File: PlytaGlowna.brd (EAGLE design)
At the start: 80 x 50 mm, 17 parts, among them X10A- CZUJ_STOP_PRAWY, X11A- CZUJNIK_STOP_LEWY, X12A- SWIATL_PRZOD, X13A- SWIATL_TYL, X1B 5566-2, X2A- STACYJKA, X3A- VOLTOMIERZ, X4A- PRZERYWACZ, X5A- WL_SWIATLA_DZIENNE, X6A- REKOJESC_LEW, X7A- KLAKSON, X8A- ZAS USB/12V, X9A- SYGNALIZATOR

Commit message: druga wyprodukowana plytka
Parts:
- removed R1, R2, R3, R4: (no value), rcl:R1206
- removed X5A-: WL_SWIATLA_DZIENNE, my_electronics_library:PCB-43045-0212
- added D1, D2: 1N4446, diode:DO35-10
- added U$1: 43045-0412, my_electronics_library:PCB-43045-0412
- added U$2: BUZZER, my_electronics_library:PCB-43045-0212
- moved X11A- 13.0 mm to (43.0, 9.00)
- moved X10A- 10.0 mm to (34.0, 9.00)
- moved X4A- 4.00 mm to (10.0, 38.0)
- moved X9A- 3.00 mm to (41.0, 25.0)
- moved X7A- 1.00 mm to (28.4, 23.8)
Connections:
- removed net N$2: R2.2, X9A-.P$2
- removed net N$3: R3.2, X9A-.P$3
- removed net N$4: R4.2, X9A-.P$5
- net +12V: no longer X6A-.P$4
- net +12V/ST: now also U$1.P$2, X6A-.P$4, X9A-.P$5; no longer R4.1, X5A-.P$1
- net DZIENNE: now also U$1.P$1; no longer X5A-.P$2
- net KIER_LEWY: now also D1.A, X9A-.P$1; no longer R1.1
- net KIER_PRAWY: now also D2.A, X9A-.P$2; no longer R2.1
- net MASA: now also U$1.P$3, U$2.P$2
- net MIJANIA: now also X9A-.P$3; no longer R3.1
- net N$1: now also D1.C, D2.C, U$2.P$1; no longer R1.2, X9A-.P$1
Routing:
- net +12V: track 57.9 -> 28.6 mm, vias 2 -> 0
- net N$1: track 13.9 -> 38.8 mm
- net MASA: track 205.9 -> 224.0 mm
- net STOP: track 24.2 -> 39.1 mm
- net KIER_LEWY: track 93.9 -> 105.9 mm, vias 2 -> 3
- net KIER_PRAWY: track 102.4 -> 114.0 mm
- net MIJANIA: track 70.4 -> 79.2 mm
- net N$4: track 6.21 -> 0.00 mm
- net N$3: track 5.08 -> 0.00 mm
- net N$2: track 5.04 -> 0.00 mm
- net DZIENNE: track 13.8 -> 18.8 mm
- net KIER_WSPOLNY: track 28.1 -> 32.1 mm
- net +12V/ST: track 148.3 -> 145.8 mm
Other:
- board text added: "rev. 002"

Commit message: czesc zmian do wersji 3
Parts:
- removed U$2: BUZZER, my_electronics_library:PCB-43045-0212
- removed X2A-: STACYJKA, my_electronics_library:PCB-43045-0212
- removed X3A-: VOLTOMIERZ, my_electronics_library:PCB-43045-0212
- removed X4A-: PRZERYWACZ, my_electronics_library:PCB-43045-0412
- added J1: PRZERYWACZ, con-molex:6410-03
- added J2: STACYJKA, con-molex:6410-02
- added J3: VOLTOMIERZ, con-molex:6410-02
- added J4: BUZZER, con-molex:6410-02
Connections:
- net +12V: now also J2.1; no longer X2A-.P$1
- net +12V/ST: now also J1.1, J2.2, J3.1; no longer X2A-.P$2, X3A-.P$1, X4A-.P$1
- net KIER_WSPOLNY: now also J1.3; no longer X4A-.P$3
- net MASA: now also J1.2, J3.2, J4.1; no longer U$2.P$2, X3A-.P$2, X4A-.P$2
- net N$1: now also J4.2; no longer U$2.P$1
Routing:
- net MASA: track 224.0 -> 231.4 mm
- net +12V/ST: track 145.8 -> 141.2 mm
- net +12V: track 28.6 -> 31.7 mm
- net N$1: track 38.8 -> 40.7 mm
- net KIER_WSPOLNY: track 32.1 -> 30.5 mm
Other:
- board text added: "rev. 003"
- board text removed: "rev. 002"

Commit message: temporary changes
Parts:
- removed U$1: 43045-0412, my_electronics_library:PCB-43045-0412
- removed X10A-: CZUJ_STOP_PRAWY, my_electronics_library:PCB-43045-0212
- removed X11A-: CZUJNIK_STOP_LEWY, my_electronics_library:PCB-43045-0212
- removed X12A-: SWIATL_PRZOD, my_electronics_library:PCB-43045-0612
- removed X13A-: SWIATL_TYL, my_electronics_library:PCB-43045-0612
- removed X7A-: KLAKSON, my_electronics_library:PCB-43045-0212
- removed X8A-: ZAS USB/12V, my_electronics_library:PCB-43045-0212
- removed X9A-: SYGNALIZATOR, my_electronics_library:PCB-43045-0612
- added J10: SWIATLA_TYL, con-molex:6410-06
- added J11: SWIATLA_PRZOD, con-molex:6410-06
- added J12: SYGNALIZATOR, con-molex:6410-06
- added J13: 22-27-2081-08, con-molex:6410-08
- added J5: KLAKSON, con-molex:6410-02
- added J6: CZUJNIK_STOP_LEWY, con-molex:6410-02
- added J7: CZUJNIK_STOP_PRAWY, con-molex:6410-02
- added J8: ZAS_USB/12V, con-molex:6410-02
- added J9: 22-27-2031-03, con-molex:6410-03
- moved J4 1.00 mm to (54.0, 9.00)
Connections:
- net +12V: now also J8.1; no longer X8A-.P$2
- net +12V/ST: now also J12.3, J6.1, J7.1, J9.1; no longer U$1.P$2, X10A-.P$1, X11A-.P$1, X9A-.P$5
- net DZIENNE: now also J11.4, J9.2; no longer U$1.P$1, X12A-.P$2
- net KIER_LEWY: now also J10.1, J11.6, J12.1; no longer X12A-.P$4, X13A-.P$6, X9A-.P$1
- net KIER_PRAWY: now also J10.3, J11.3, J12.2; no longer X12A-.P$5, X13A-.P$5, X9A-.P$2
- net KLAKSON: now also J5.1; no longer X7A-.P$2
- net MASA: now also J10.5, J10.6, J11.1, J11.2, J12.5, J5.2, J8.2, J9.3; no longer U$1.P$3, X12A-.P$6, X13A-.P$4, X7A-.P$1, X8A-.P$1, X9A-.P$6
- net MIJANIA: now also J10.2, J11.5, J12.6; no longer X12A-.P$1, X13A-.P$3, X9A-.P$3
- net STOP: now also J10.4, J6.2, J7.2; no longer X10A-.P$2, X11A-.P$2, X13A-.P$2
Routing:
- net KIER_LEWY: track 105.9 -> 97.0 mm
- net STOP: track 39.1 -> 41.5 mm
- net KIER_PRAWY: track 114.0 -> 116.1 mm
- net MASA: track 231.4 -> 233.5 mm
- net DZIENNE: track 18.8 -> 20.8 mm
- net +12V/ST: track 141.2 -> 143.0 mm
- net KLAKSON: track 15.3 -> 17.0 mm
- net N$1: track 40.7 -> 39.7 mm
- net +12V: track 31.7 -> 31.0 mm

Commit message: rev.003 RC1
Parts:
- removed X6A-: REKOJESC_LEW, my_electronics_library:PCB-43045-0812
- added D3, D4: 1N4446, diode:DO35-10
- moved J13 15.8 mm to (27.0, 42.0)
- moved J1 3.00 mm to (10.0, 42.0), turned to 180 degrees
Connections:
- new net N$2: D3.C, J10.4
- new net N$3: D4.C, J10.2
- net +12V/ST: now also J1.3, J13.1, J13.2, J13.3; no longer J1.1, X6A-.P$1, X6A-.P$4
- net KIER_LEWY: now also J13.7; no longer X6A-.P$7
- net KIER_PRAWY: now also J13.8; no longer X6A-.P$5
- net KIER_WSPOLNY: now also J1.1, J13.4; no longer J1.3, X6A-.P$6
- net KLAKSON: now also J13.5; no longer X6A-.P$3
- net MIJANIA: now also D4.A, J13.6; no longer J10.2, X6A-.P$2
- net STOP: now also D3.A; no longer J10.4
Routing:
- net +12V/ST: track 143.0 -> 122.8 mm, vias 2 -> 0
- net STOP: track 41.5 -> 30.2 mm
- net MIJANIA: track 78.8 -> 68.4 mm
- net N$2: track 0.00 -> 9.16 mm
- net N$3: track 0.00 -> 6.37 mm
- net KIER_LEWY: track 97.0 -> 92.1 mm
- net KIER_PRAWY: track 116.1 -> 112.4 mm
- net KIER_WSPOLNY: track 30.5 -> 27.3 mm
- net MASA: track 233.5 -> 230.9 mm
- net KLAKSON: track 17.0 -> 18.6 mm

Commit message: rev.003 RC2
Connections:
- net N$2 renamed STOP_DIODE
- net N$3 renamed MIJANIA_DIODE
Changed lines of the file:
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@@
 <wire x1="55.27" y1="11.77" x2="57" y2="13.5" width="1.5" layer="16"/>
 </signal>
-<signal name="N$2">
+<signal name="STOP_DIODE">
 <contactref element="D3" pad="C"/>
 <contactref element="J10" pad="4"/>
@@
 <wire x1="63.73" y1="9.73" x2="60.92" y2="6.92" width="1.5" layer="16"/>
 </signal>
-<signal name="N$3">
+<signal name="MIJANIA_DIODE">
 <contactref element="D4" pad="C"/>
 <contactref element="J10" pad="2"/>

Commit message: poprawki diod, ver.003 RC3
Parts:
- D1, D4: value 1N4446 -> 1N4004; device diode:DO35-10 -> diode:DO41-10
- D2, D3: value 1N4446 -> BYV28-200; device diode:DO35-10 -> diode:SOD64-10
- moved D2 29.7 mm to (56.0, 13.0), turned to 90 degrees
- moved D4 22.4 mm to (65.0, 41.0), turned to 0 degrees
- moved D3 7.07 mm to (60.0, 19.0)
- moved J4 4.00 mm to (50.0, 9.00)
- moved D1 3.61 mm to (69.0, 38.0)
- moved J6 2.00 mm to (43.0, 9.00)
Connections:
- net KIER_LEWY: now also D4.A; no longer D1.A
- net KIER_PRAWY: now also D1.A; no longer D2.A
- net MIJANIA: now also D3.A; no longer D4.A
- net MIJANIA_DIODE: now also D3.C; no longer D4.C
- net N$1: now also D4.C; no longer D2.C
- net STOP: now also D2.A; no longer D3.A
- net STOP_DIODE: now also D2.C; no longer D3.C
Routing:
- net STOP: track 30.2 -> 26.0 mm
- net STOP_DIODE: track 9.16 -> 11.5 mm
- net KIER_LEWY: track 92.1 -> 93.9 mm
- net KIER_PRAWY: track 112.4 -> 111.2 mm
- net DZIENNE: track 20.8 -> 21.9 mm
- net MIJANIA_DIODE: track 6.37 -> 7.37 mm
- net N$1: track 39.7 -> 39.2 mm

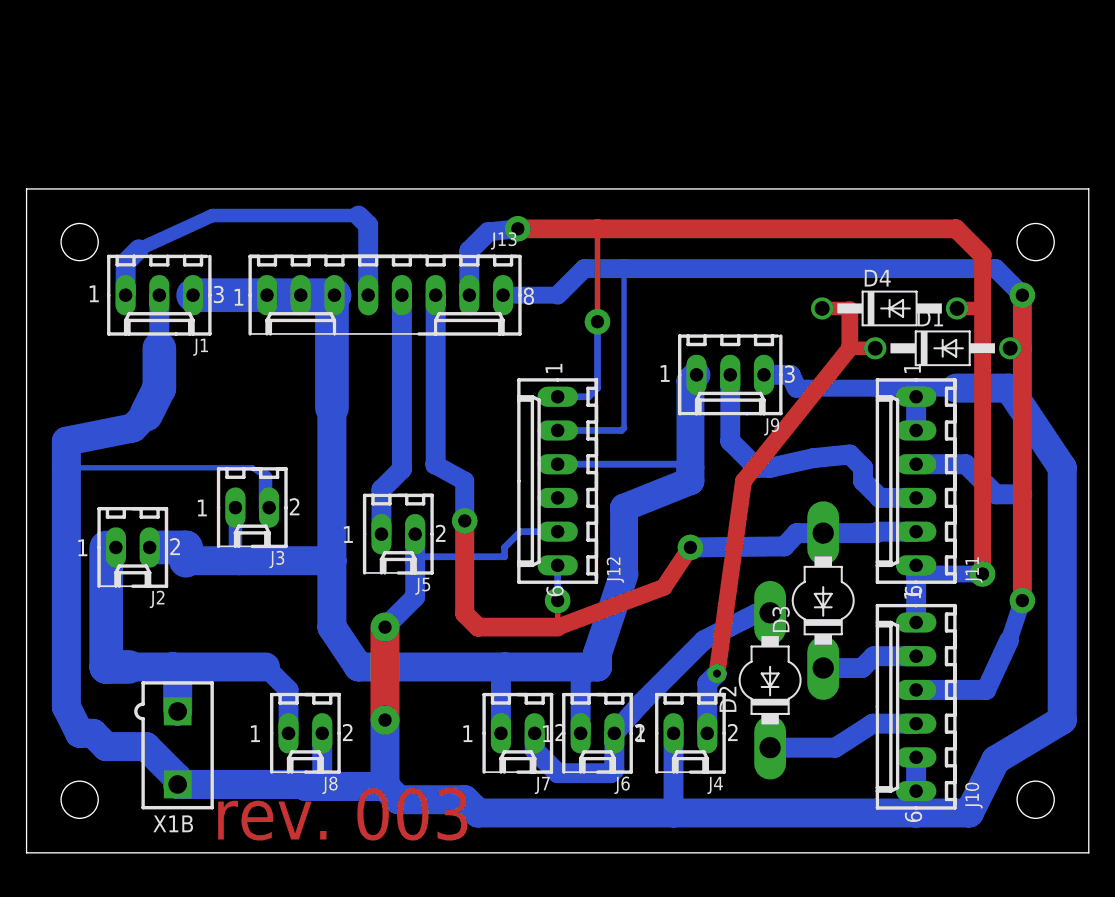
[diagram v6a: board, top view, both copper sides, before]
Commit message: poprawki routingu sciezek, ver.003 RC4
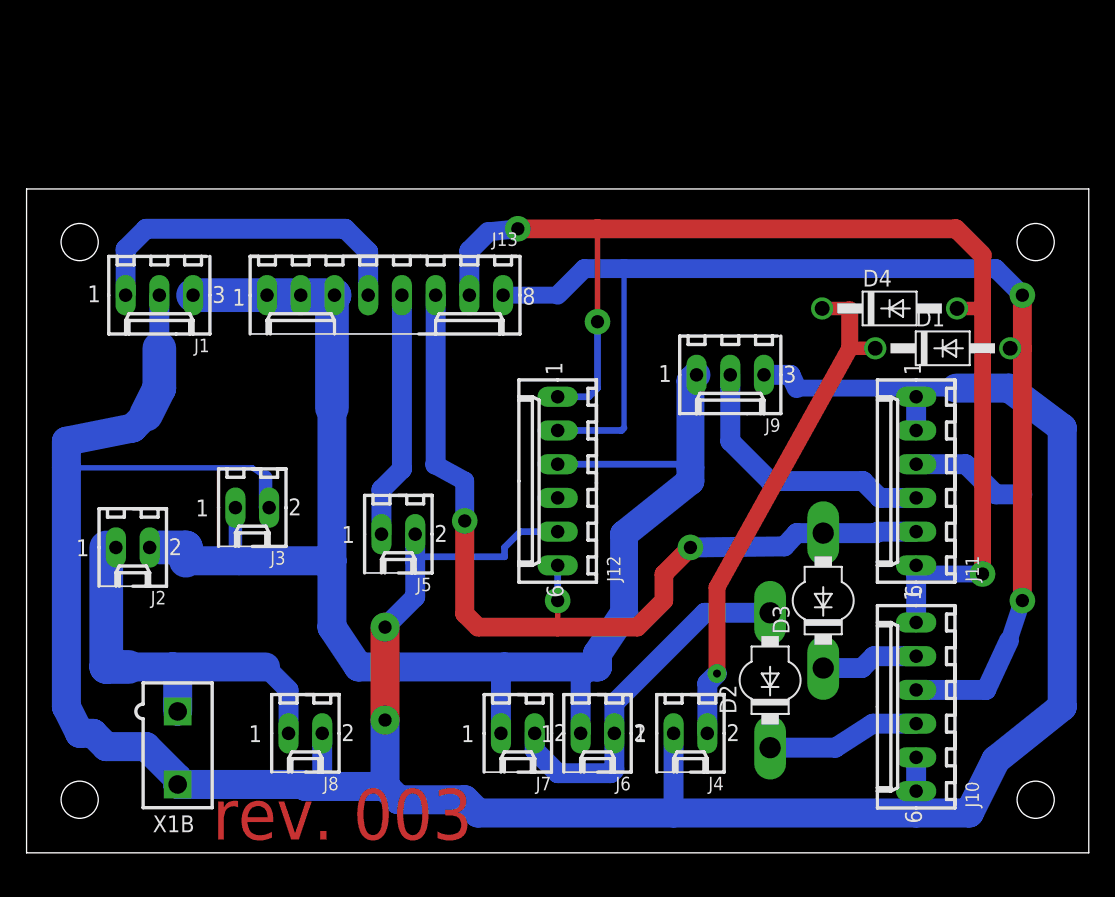
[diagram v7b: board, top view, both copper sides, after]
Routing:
- net STOP: track 26.0 -> 27.6 mm
- net MIJANIA: track 68.0 -> 69.5 mm
- net DZIENNE: track 21.9 -> 20.8 mm
- net KIER_WSPOLNY: track 27.3 -> 26.4 mm
- net +12V/ST: track 123.2 -> 122.5 mm
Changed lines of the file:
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@@
 <wire x1="71" y1="3" x2="73" y2="7" width="2.1844" layer="16"/>
 <wire x1="70" y1="35" x2="74" y2="35" width="2.1844" layer="16"/>
-<wire x1="74" y1="35" x2="78" y2="29" width="2.1844" layer="16"/>
-<wire x1="78" y1="29" x2="78" y2="10" width="2.1844" layer="16"/>
-<wire x1="78" y1="10" x2="73" y2="7" width="2.1844" layer="16"/>
+<wire x1="74" y1="35" x2="78" y2="32" width="2.1844" layer="16"/>
+<wire x1="78" y1="32" x2="78" y2="11" width="2.1844" layer="16"/>
+<wire x1="78" y1="11" x2="73" y2="7" width="2.1844" layer="16"/>
 <wire x1="11.38" y1="5.15" x2="11.38" y2="5.62" width="2.1844" layer="16"/>
 <wire x1="11.38" y1="5.62" x2="9" y2="8" width="2.1844" layer="16"/>
@@
 <wire x1="36" y1="14" x2="43" y2="14" width="2.1844" layer="16"/>
 <wire x1="43" y1="14" x2="43" y2="15" width="2.1844" layer="16"/>
-<wire x1="43" y1="15" x2="45" y2="21" width="2.1844" layer="16"/>
+<wire x1="43" y1="15" x2="45" y2="18" width="2.1844" layer="16"/>
 <contactref element="J2" pad="2"/>
 <wire x1="12" y1="22" x2="12" y2="23" width="2.54" layer="16"/>
@@
 <wire x1="41.73" y1="13.27" x2="43" y2="14" width="1.5" layer="16"/>
 <contactref element="J9" pad="1"/>
-<wire x1="45" y1="21" x2="45" y2="26" width="2.1" layer="16"/>
-<wire x1="45" y1="26" x2="50" y2="28" width="2.1" layer="16"/>
+<wire x1="45" y1="18" x2="45" y2="24" width="2.1" layer="16"/>
+<wire x1="45" y1="24" x2="50" y2="28" width="2.1" layer="16"/>
 <wire x1="50" y1="28" x2="50" y2="29" width="2.1" layer="16"/>
 <wire x1="50" y1="29" x2="50" y2="35.54" width="2.1" layer="16"/>
@@
 <wire x1="33" y1="18" x2="34" y2="17" width="1.4224" layer="1"/>
 <via x="50" y="23" extent="1-16" drill="1" diameter="1.9304"/>
-<wire x1="34" y1="17" x2="40" y2="17" width="1.4224" layer="1"/>
 <wire x1="40" y1="20" x2="40" y2="19" width="0.4064" layer="16"/>
 <via x="40" y="19" extent="1-16" drill="1" diameter="1.9304"/>
-<wire x1="40" y1="19" x2="40" y2="17" width="0.4064" layer="1"/>
-<wire x1="50" y1="23" x2="48" y2="20" width="1.27" layer="1"/>
-<wire x1="48" y1="20" x2="40" y2="17" width="1.27" layer="1"/>
+<wire x1="40" y1="17" x2="40" y2="19" width="0.4064" layer="1"/>
 <contactref element="J11" pad="5"/>
 <contactref element="J12" pad="6"/>
@@
 <wire x1="60" y1="24.08" x2="58" y2="24.08" width="1.5" layer="16"/>
 <wire x1="58" y1="24.08" x2="57.08" y2="23.08" width="1.5" layer="16"/>
+<wire x1="34" y1="17" x2="40" y2="17" width="1.4" layer="1"/>
+<wire x1="50" y1="23" x2="48" y2="21" width="1.4" layer="1"/>
+<wire x1="48" y1="21" x2="48" y2="19" width="1.4" layer="1"/>
+<wire x1="48" y1="19" x2="46" y2="17" width="1.4" layer="1"/>
+<wire x1="46" y1="17" x2="40" y2="17" width="1.4" layer="1"/>
 </signal>
 <signal name="KIER_WSPOLNY">
-<wire x1="14" y1="48" x2="25" y2="48" width="1.016" layer="16"/>
-<wire x1="8.46" y1="45.46" x2="14" y2="48" width="1.016" layer="16"/>
 <contactref element="J13" pad="4"/>
-<wire x1="25.73" y1="42" x2="25.73" y2="47.27" width="1.5" layer="16"/>
-<wire x1="25.73" y1="47.27" x2="25" y2="48" width="1.5" layer="16"/>
 <contactref element="J1" pad="1"/>
-<wire x1="7.46" y1="42" x2="7.46" y2="44.46" width="1.5" layer="16"/>
-<wire x1="7.46" y1="44.46" x2="8.46" y2="45.46" width="1.5" layer="16"/>
+<wire x1="7.46" y1="42" x2="7.46" y2="45.46" width="1.5" layer="16"/>
+<wire x1="9" y1="47" x2="7.46" y2="45.46" width="1.5" layer="16"/>
+<wire x1="25.73" y1="42" x2="25.73" y2="45.27" width="1.5" layer="16"/>
+<wire x1="25.73" y1="45.27" x2="24" y2="47" width="1.5" layer="16"/>
+<wire x1="24" y1="47" x2="9" y2="47" width="1.5" layer="16"/>
 </signal>
 <signal name="KIER_LEWY">
@@
 <signal name="DZIENNE">
 <contactref element="J9" pad="2"/>
+<contactref element="J11" pad="4"/>
 <wire x1="53" y1="36" x2="53" y2="31" width="1.5" layer="16"/>
-<wire x1="53" y1="31" x2="55" y2="29" width="1.5" layer="16"/>
-<wire x1="56" y1="29" x2="55" y2="29" width="1.5" layer="16"/>
-<contactref element="J11" pad="4"/>
+<wire x1="53" y1="31" x2="56" y2="28" width="1.5" layer="16"/>
+<wire x1="63" y1="28" x2="56" y2="28" width="1.5" layer="16"/>
 <wire x1="67" y1="26.73" x2="64.27" y2="26.73" width="1.5" layer="16"/>
 <wire x1="64.27" y1="26.73" x2="63" y2="28" width="1.5" layer="16"/>
-<wire x1="63" y1="28" x2="63" y2="29" width="1.5" layer="16"/>
-<wire x1="63" y1="29" x2="62" y2="30" width="1.5" layer="16"/>
-<wire x1="62" y1="30" x2="59.27" y2="29.73" width="1.5" layer="16"/>
-<wire x1="59.27" y1="29.73" x2="56" y2="29" width="1.5" layer="16"/>
 </signal>
 <signal name="STOP">
@@
 <wire x1="44" y1="6" x2="44.27" y2="6.27" width="1.5" layer="16"/>
 <wire x1="44.27" y1="6.27" x2="44.27" y2="9" width="1.5" layer="16"/>
-<wire x1="44.27" y1="9" x2="46.27" y2="11.27" width="1.5" layer="16"/>
-<wire x1="46.27" y1="11.27" x2="51" y2="16" width="1.5" layer="16"/>
-<wire x1="52.92" y1="17" x2="51" y2="16" width="1.5" layer="16"/>
 <contactref element="D2" pad="A"/>
-<wire x1="56" y1="18.08" x2="54.92" y2="18" width="1.5" layer="16"/>
-<wire x1="54.92" y1="18" x2="52.92" y2="17" width="1.5" layer="16"/>
+<wire x1="44.27" y1="9" x2="44.27" y2="11.27" width="1.5" layer="16"/>
+<wire x1="51.08" y1="18.08" x2="56" y2="18.08" width="1.5" layer="16"/>
+<wire x1="44.27" y1="11.27" x2="51.08" y2="18.08" width="1.5" layer="16"/>
 </signal>
 <signal name="N$1">
-<wire x1="54" y1="28" x2="62" y2="38" width="1.27" layer="1"/>
+<wire x1="52" y1="20" x2="62" y2="38" width="1.27" layer="1"/>
 <wire x1="62" y1="40.92" x2="62" y2="38" width="1.27" layer="1"/>
-<wire x1="54" y1="28" x2="52" y2="13.5" width="1.27" layer="1"/>
+<wire x1="52" y1="20" x2="52" y2="13.5" width="1.27" layer="1"/>
 <via x="52" y="13.5" extent="1-16" drill="0.6" diameter="1.4224" shape="octagon"/>
 <contactref element="J4" pad="2"/>
